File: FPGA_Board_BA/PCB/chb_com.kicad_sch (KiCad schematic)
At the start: 9 parts, among them J12 Box_Header_2x05_THT, J13 Box_Header_2x05_THT, J14 Box_Header_2x05_THT, J15 Box_Header_2x05_THT, J18 Plug_Terminal_2x12pin, U26 BoxHeader_24pin, U45 BoxHeader_24pin, U46 BoxHeader_24pin, U47 BoxHeader_24pin

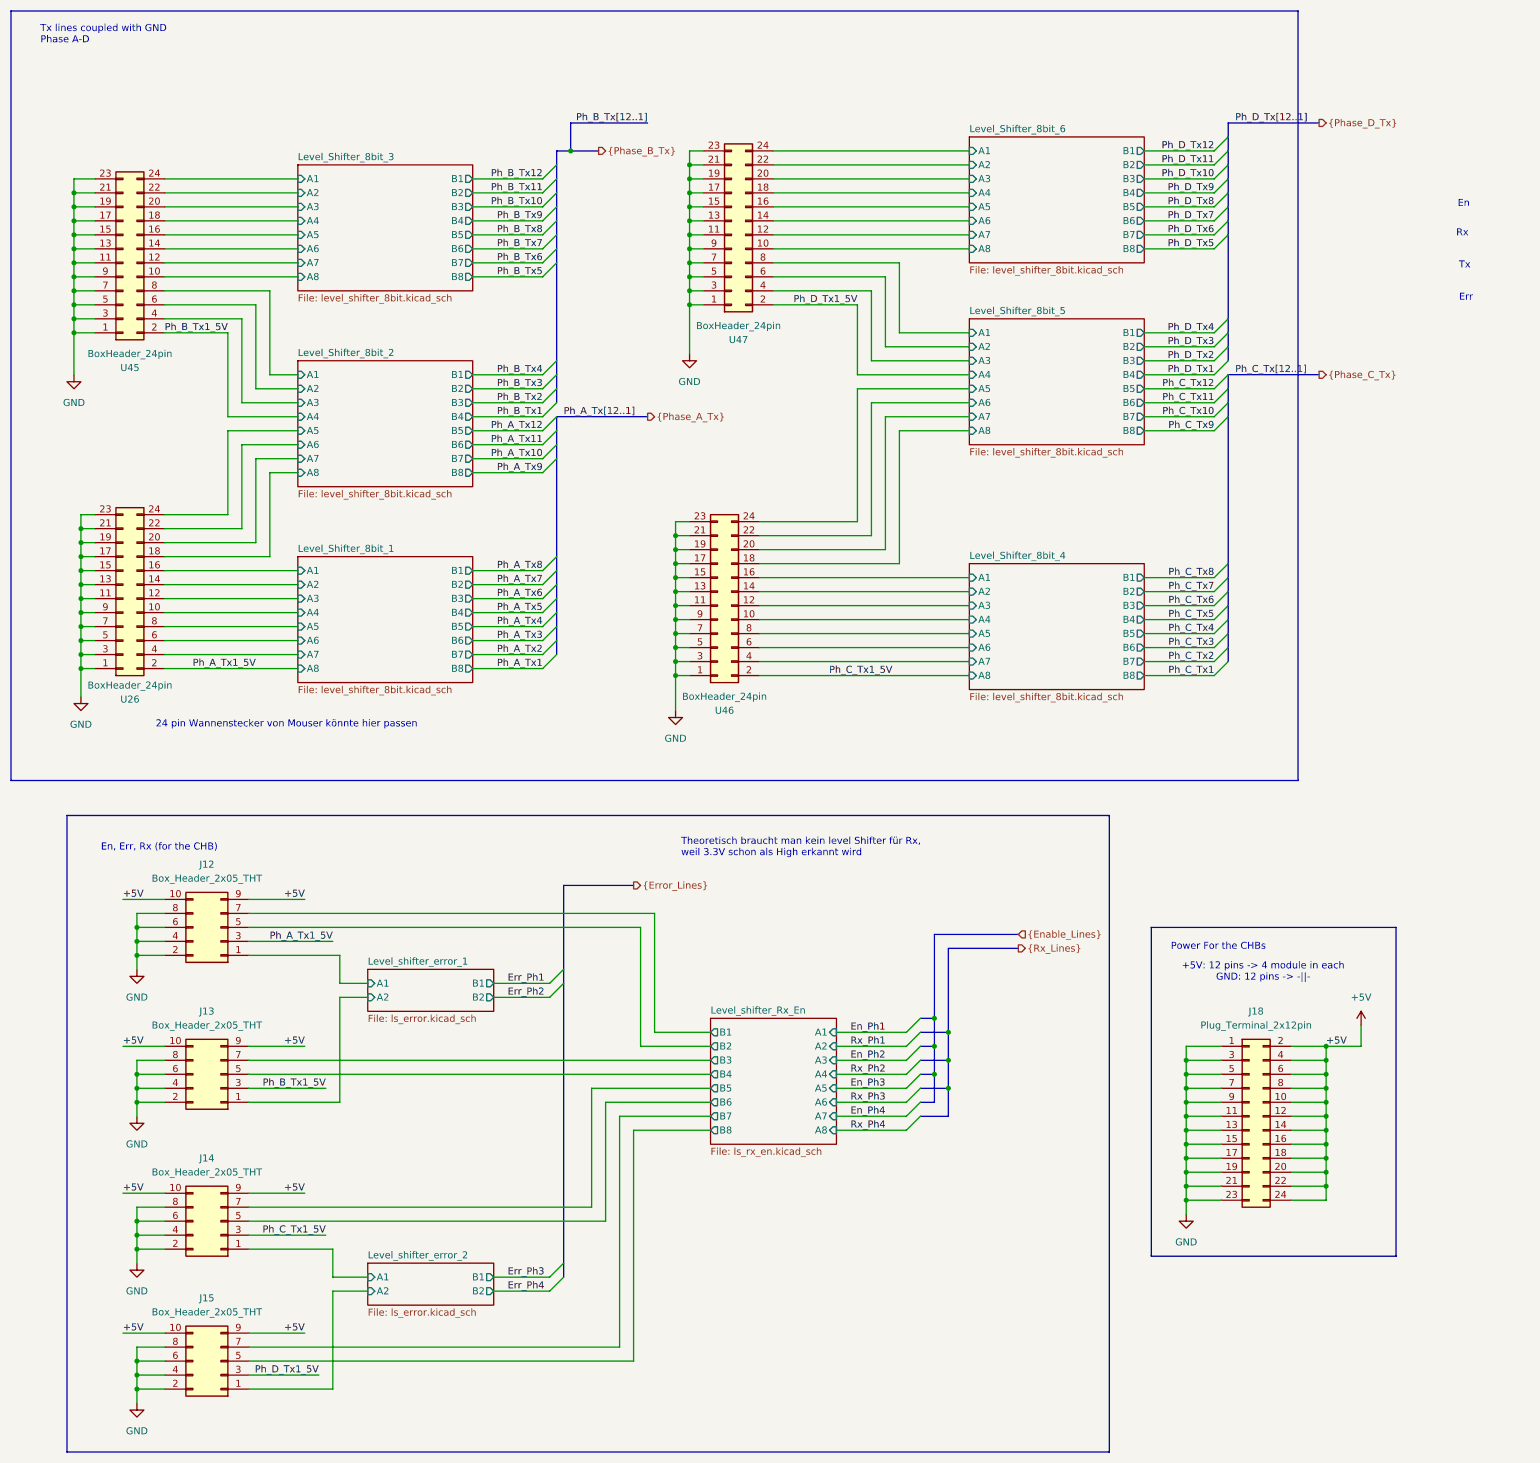
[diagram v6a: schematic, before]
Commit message: final layout almost ready (onlypower is left)
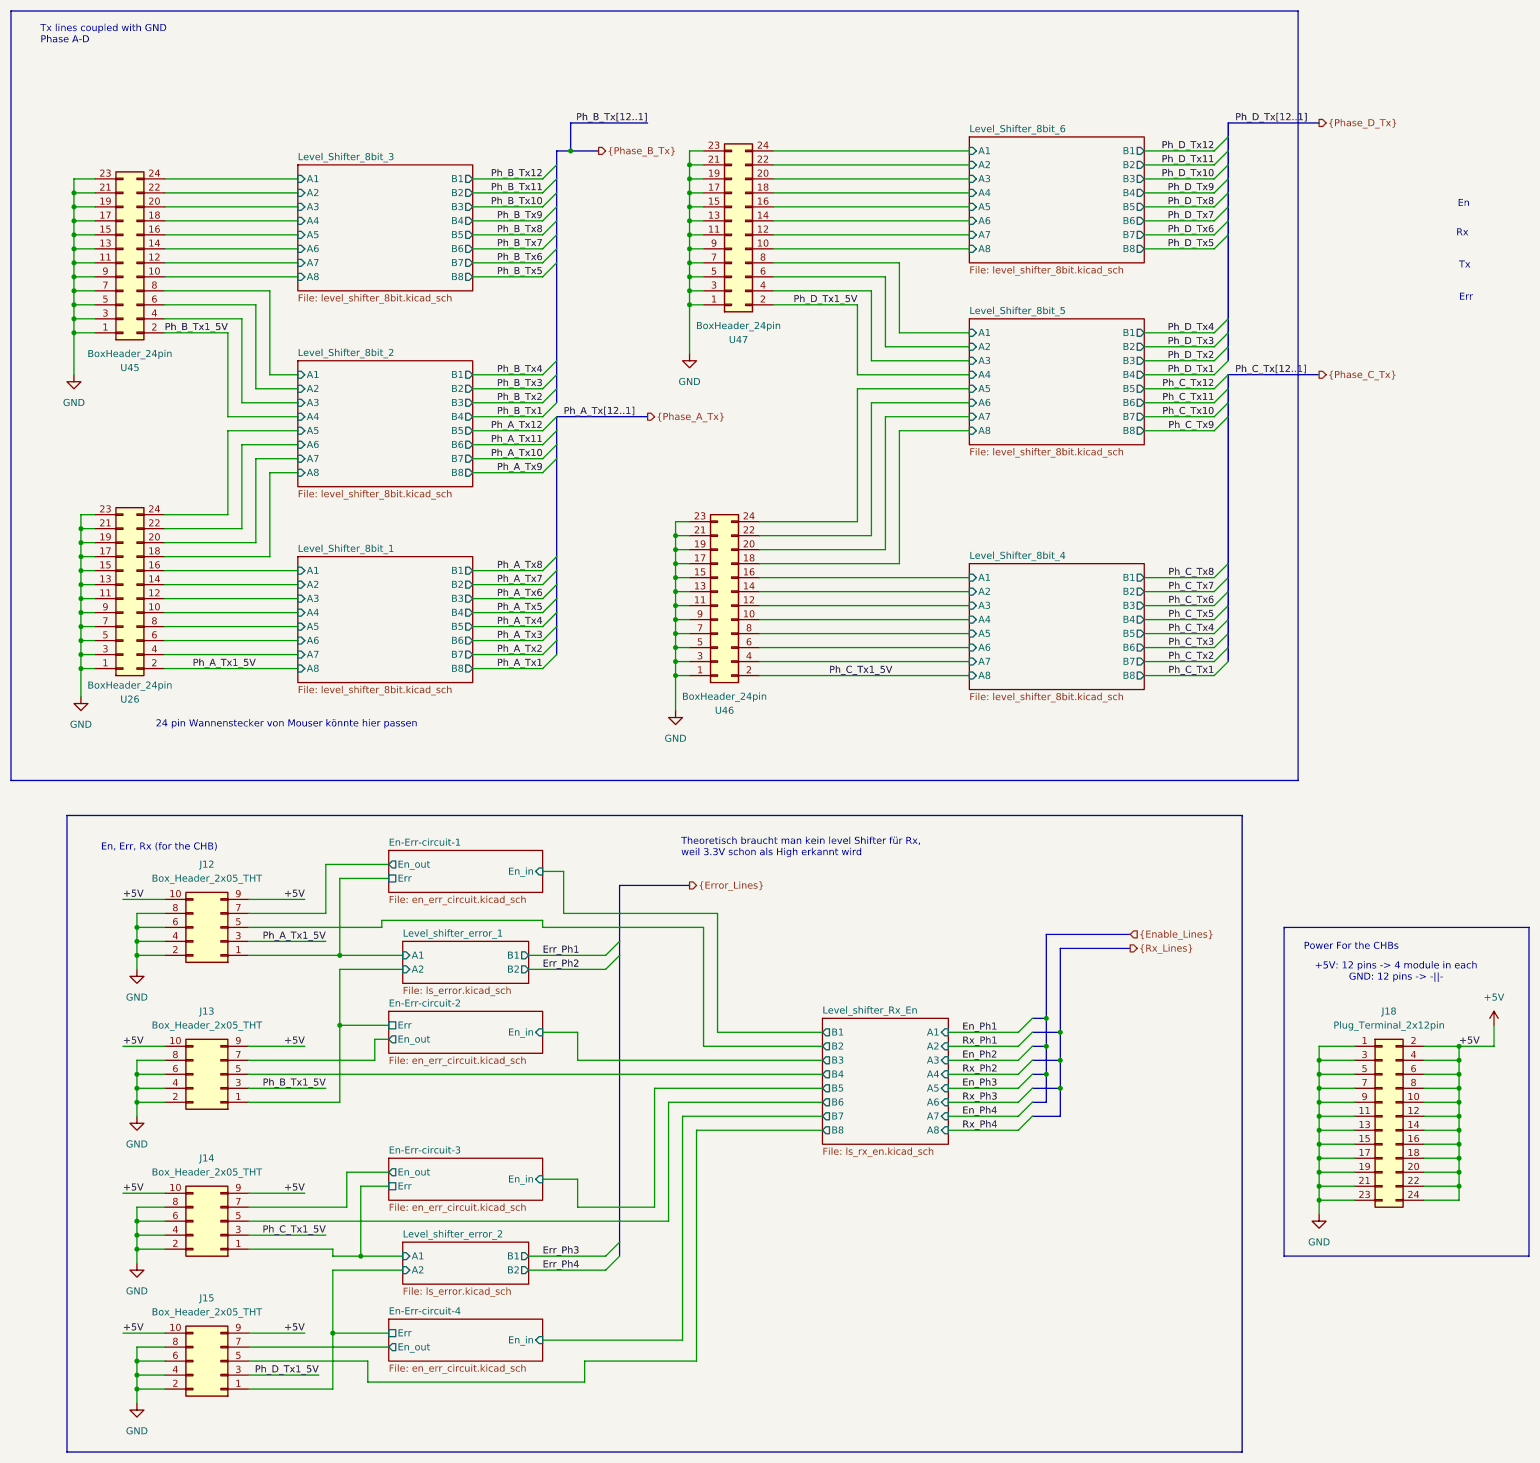
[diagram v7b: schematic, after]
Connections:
- net Level_shifter_Rx_En/B1 renamed En-Err-circuit-1/En_out
- net Level_shifter_Rx_En/B3 renamed En-Err-circuit-2/En_out
- net Level_shifter_Rx_En/B5 renamed En-Err-circuit-3/En_out
- net Level_shifter_Rx_En/B7 renamed En-Err-circuit-4/En_out
- net Level_shifter_error_1/A1 renamed En-Err-circuit-1/Err
- net Level_shifter_error_1/A2 renamed En-Err-circuit-2/Err
- net Level_shifter_error_2/A1 renamed En-Err-circuit-3/Err
- net Level_shifter_error_2/A2 renamed En-Err-circuit-4/Err
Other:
- added sheet En-Err-circuit-1 (en_err_circuit.kicad_sch)
- added sheet En-Err-circuit-2 (en_err_circuit.kicad_sch)
- added sheet En-Err-circuit-3 (en_err_circuit.kicad_sch)
- added sheet En-Err-circuit-4 (en_err_circuit.kicad_sch)
- moved on the sheet: J18
